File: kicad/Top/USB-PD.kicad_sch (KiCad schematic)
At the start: 43 parts, among them J4 USBC_Receptacle_SMD_RA, J6 M20-9990246, Q6 SI4477DY-T1-GE3, Q7 SI4477DY-T1-GE3

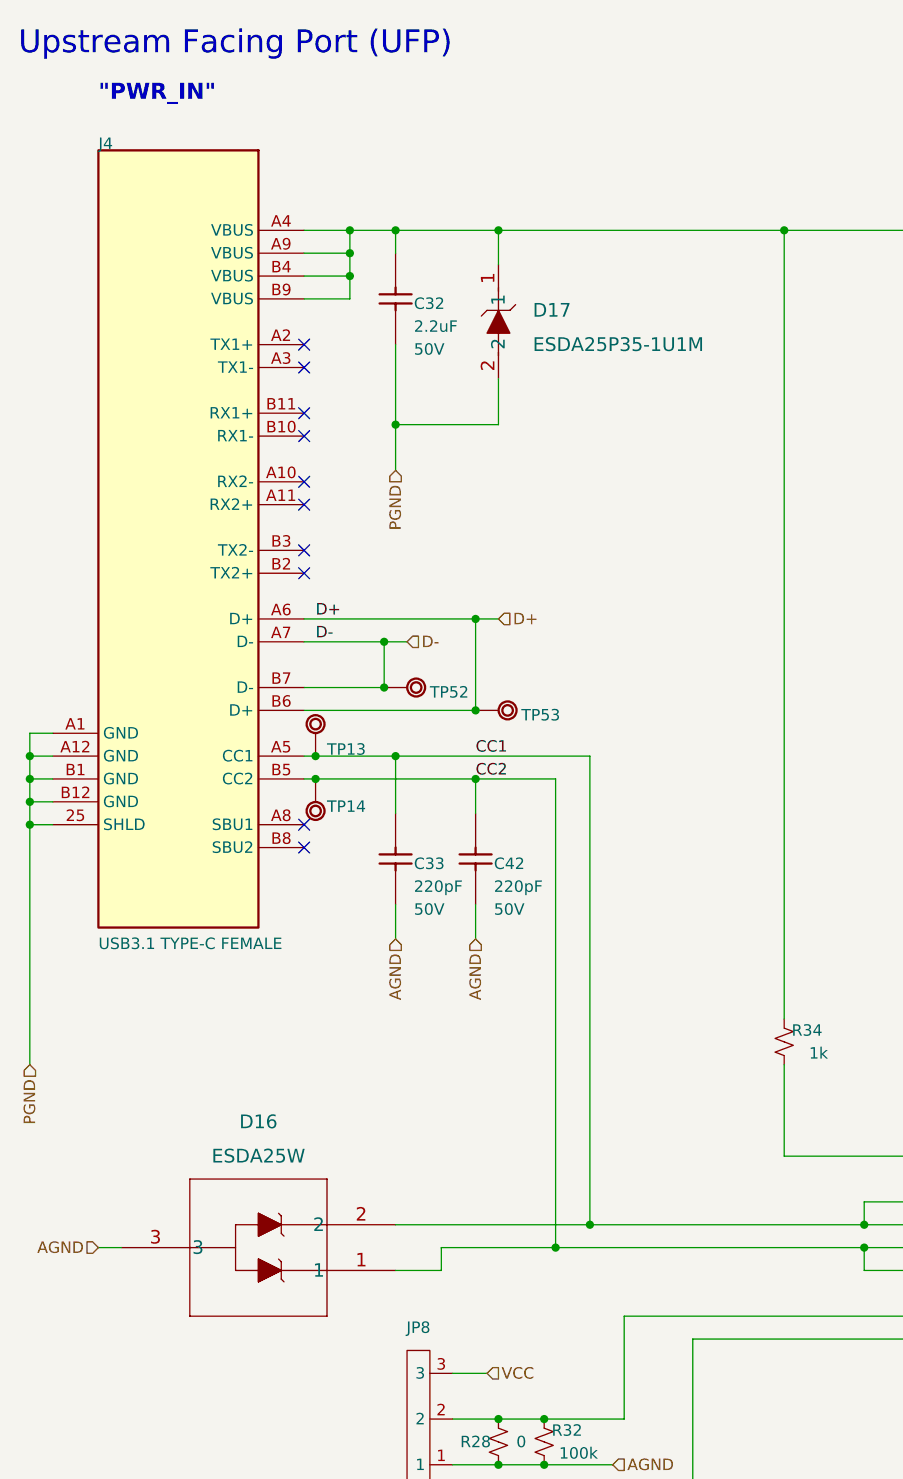
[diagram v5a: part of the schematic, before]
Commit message: Added hierarchial pins to mcu
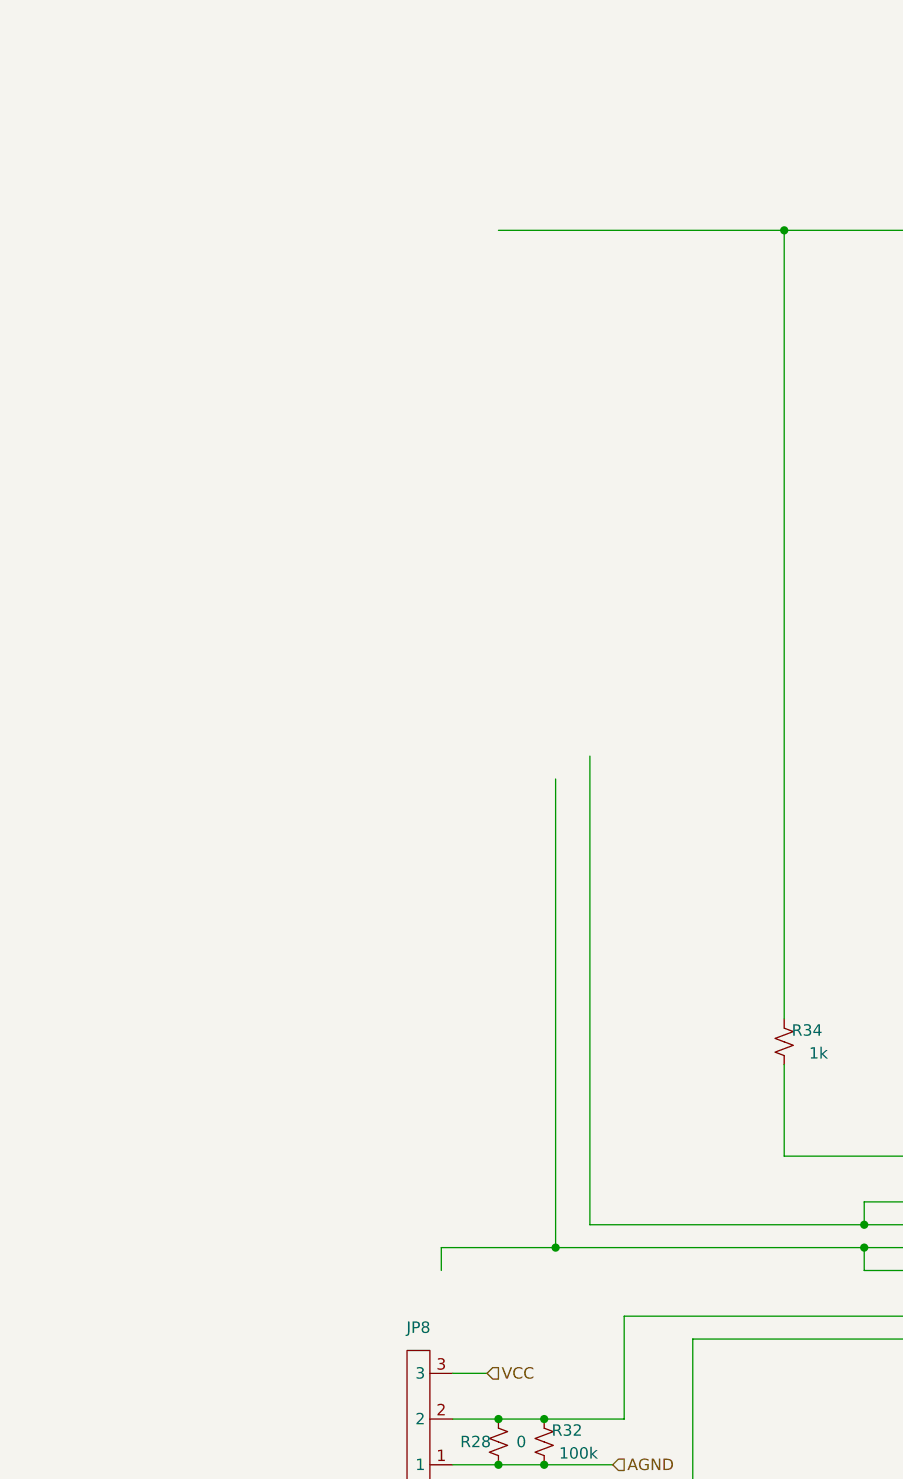
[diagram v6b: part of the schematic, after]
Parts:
- removed C32: Capacitor NP, AltiumImports:_ALTIUM_WORK_00001_MCHP-CDB_Library_Database_MCHP-CDB.DbLib_Capacitor_CAP_C_0603, symbol Top-altium-import:1_Capacitor NP
- removed C33, C42: Capacitor NP, AltiumImports:_ALTIUM_WORK_00001_MCHP-CDB_Library_Database_MCHP-CDB.DbLib_Capacitor_CAP_C_0402, symbol Top-altium-import:1_Capacitor NP
- removed D16: ESDA25W, custom_modules:ESDA25W, symbol ESDA25W:ESDA25W
- removed D17: ESDA25P35-1U1M, custom_modules:ESDA25P35-1U1M, symbol ESDA25P35-1U1M:ESDA25P35-1U1M
- removed J4: USBC_Receptacle_SMD_RA, AltiumImports:CON_USB3.1-C_RCPT_SMD_RA_ACP_12401610E4#2A, symbol Top-altium-import:0_mirrored_USBC_Receptacle_SMD_RA
- removed TP13: Test Point No BOM, AltiumImports:_ALTIUM_WORK_00001_MCHP-CDB_Library_Database_.._Footprints_TP_1mm_SMD.PcbLib_TP_1mm_SMD, symbol Top-altium-import:1_Test Point No BOM
- removed TP14: Test Point No BOM, AltiumImports:_ALTIUM_WORK_00001_MCHP-CDB_Library_Database_.._Footprints_TP_1mm_SMD.PcbLib_TP_1mm_SMD, symbol Top-altium-import:3_Test Point No BOM
- removed TP52, TP53: Test Point No BOM, AltiumImports:_ALTIUM_WORK_00001_MCHP-CDB_Library_Database_.._Footprints_TP_1mm_SMD.PcbLib_TP_1mm_SMD, symbol Top-altium-import:0_Test Point No BOM
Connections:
- net CC1: no longer names the net of U?.1 (CC1DB), U?.2 (CC1)
- net CC2: no longer names the net of U?.4 (CC2), U?.5 (CC2DB)
- no-connect marks 12 -> 2
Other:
- note removed: ""PWR_IN""
- note removed: "Upstream Facing Port (UFP)"

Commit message: wip started working on pd sheet but need more info before proceeding
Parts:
- removed C43, C44, C45: 1uF, symbol Device:C_Small
- removed C46: 100nF, symbol Device:C_Small
- removed D18, D19, D20, D21: LED, symbol Device:LED
- removed D22: ESDA25P35-1U1M, custom_modules:ESDA25P35-1U1M, symbol ESDA25P35-1U1M:ESDA25P35-1U1M
- removed J6: M20-9990246, AltiumImports:FP-M20-9990246-MFG, symbol Top-altium-import:3_mirrored_3bc925449376181038e59eaffc5286c
- removed JP17, JP8: 3-pad-selection, symbol custom_connectors:3-pad-selection
- removed JP18: Jumper_2_Bridged, symbol Jumper:Jumper_2_Bridged
- removed Q6: SI4477DY-T1-GE3, AltiumImports:_ALTIUM_WORK_00001_MCHP-CDB_Library_Database_.._Footprints_SOIC-8.PcbLib_SOIC-8, symbol Top-altium-import:1_mirrored_SI4477DY-T1-GE3
- removed Q7: SI4477DY-T1-GE3, AltiumImports:_ALTIUM_WORK_00001_MCHP-CDB_Library_Database_.._Footprints_SOIC-8.PcbLib_SOIC-8, symbol Top-altium-import:1_SI4477DY-T1-GE3
- removed R28, R31: 0, symbol Device:R_Small_US
- removed R32, R33: 100k, symbol Device:R_Small_US
- removed R34: 1k, symbol Device:R_Small_US
- removed R35: 10K, symbol Device:R_Small_US
- removed R36: 22k, symbol Device:R_Small_US
- removed R37: Resistor, AltiumImports:_ALTIUM_WORK_00001_MCHP-CDB_Library_Database_.._Footprints_RES_C_0402.PcbLib_RES_C_0402, symbol Top-altium-import:1_Resistor
- removed R38, R47, R51: 4.7k, symbol Device:R_Small_US
- removed R48, R49, R50, R54: ?, symbol Device:R_Small_US
- removed R52: Resistor, AltiumImports:_ALTIUM_WORK_00001_MCHP-CDB_Library_Database_.._Footprints_RES_C_0402.PcbLib_RES_C_0402, symbol Top-altium-import:0_Resistor
- removed R53: 100, symbol Device:R_Small_US
- removed U?: STUSB4500QTR, Ultra_Librarian:QFN24EP_4X4_STM, symbol ultralibrarian:STUSB4500QTR
- added U?: MAX77958EWV+T, Ultra_Librarian:MAX77958EWV&plus_T, symbol ultralibrarian:MAX77958EWV+T
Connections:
- no-connect marks 2 -> 0
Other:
- note removed: ""PWR_OUT""
- note removed: "+"
- note removed: "PWR"
- note removed: "Power Output"

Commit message: Added eval board based schematic for max77958
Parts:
- added C? (x2): 27pF, symbol Device:C
- added C? (x7): 1uF, symbol Device:C
- added C?: 2.2uF, symbol Device:C
- added D? (x2): 4V, symbol Device:D_TVS
- added R? (x4): 2.2k, symbol Device:R
- added R? (x2): 1, symbol Device:R
- added R? (x4): 24, symbol Device:R
- added R?: 200k, symbol Device:R
- added R? (x2): 120k, symbol Device:R
- added R? (x2): 649k, symbol Device:R
- added TP? (x13): TestPoint_keystone, TestPoint:TestPoint_Keystone_5000-5004_Miniature, symbol custom_connectors:TestPoint_keystone
- added TP? (x7): TestPoint_CurrentShunt, custom_connectors:2.54mm_2pointCurrentTestPoint, symbol custom_connectors:TestPoint_CurrentShunt
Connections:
- net CC1: now also U?.A3 (CC1), C?.1, TP?.1
- net CC2: now also U?.A4 (CC2), C?.1, TP?.1
- net CHGIN: now also TP?.1
- net SCL_M: now also R?.1
- net SDA_M: now also R?.2
- net INTB_SL: now reaches U?.A1 (INTB)
- net INTB_SL: now also R?.2, TP?.1
- net at U?.A2 (VDD1P1): now also C?.1
- net at U?.A5 (VCIN): now also C?.1, TP?.2
- net at U?.A6 (VBUS): now also C?.1, TP?.2
- net VIO1_: now reaches U?.B1 (VIO1)
- net VIO1_: now also C?.1, R?.1, R?.1, R?.1, TP?.1, TP?.1
- net at U?.B2 (SCL): now also TP?.1, TP?.1
- net at U?.B3 (SDA): now also TP?.1, TP?.1
- net GPIO1: now reaches U?.B4 (GPIO1)
- net GPIO1: now also R?.1, R?.2
- net at U?.B5 (VDD1P8): now also C?.1
- net at U?.B6 (SYS): now also C?.1, TP?.2
- net VIO2_: now reaches U?.C1 (VIO2)
- net VIO2_: now also C?.1, R?.1, R?.1, TP?.1, TP?.1
- net at U?.C2 (SCL_M): now also R?.2, R?.2
- net at U?.C3 (SDA_M): now also R?.1, R?.2
- net GND: now reaches U?.C5 (GND_A)
- net GND: now also U?.D4 (GPIO6), U?.D6 (GND_D), C?.2, C?.2, C?.2, C?.2, C?.2, C?.2, C?.2, C?.2, C?.2, C?.2, D?.2 (A2), D?.2 (A2), TP?.1, TP?.1
- net at U?.C6 (AVL): now also C?.1
- net at U?.D1 (DN): now also R?.2
- net at U?.D2 (DP): now also R?.2
- net GPIO3: now reaches U?.D5 (GPIO3)
- net GPIO3: now also R?.1, R?.1
- net DN1: now reaches U?.E1 (DN1)
- net DN1: now also TP?.1
- net DP2: now reaches U?.E2 (DP2)
- net DP2: now also TP?.1
- net GPIO0: now reaches U?.E6 (GPIO0)
- net GPIO0: now also R?.1, R?.2
- new net: D?.1 (A1), R?.1, TP?.1 (x2)
- new net: R?.2, TP?.2 (x2)
- new net 5V: TP?.1
- new net SBU1: R?.2
- new net SBU2: R?.2
- new net SCL_SL: R?.1, R?.2
- new net SDA_SL: R?.1, R?.2
- new net SYS: TP?.1
- new net VIO1: TP?.2
- new net VIO2: TP?.2
- no-connect marks 0 -> 5
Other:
- moved on the sheet: U?
